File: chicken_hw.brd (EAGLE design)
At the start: 25.7 x 38.1 mm, 3 parts

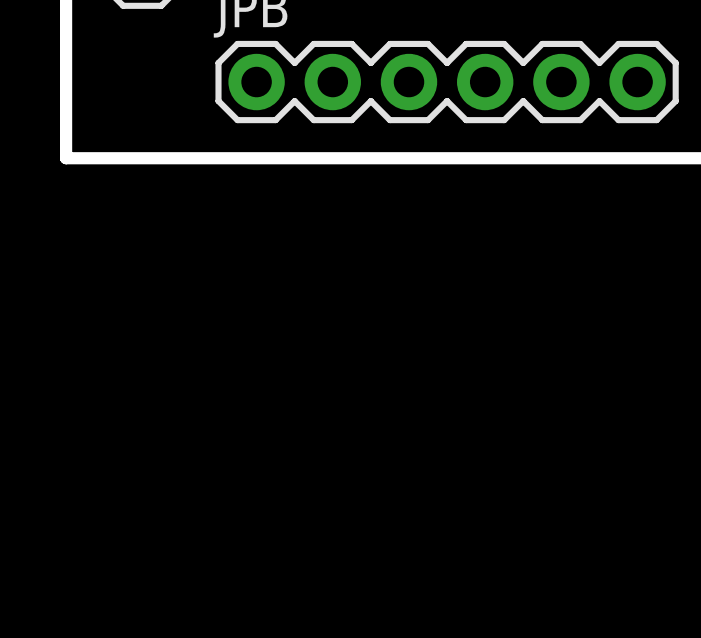
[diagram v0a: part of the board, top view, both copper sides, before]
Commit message: Start adding analog mux to design
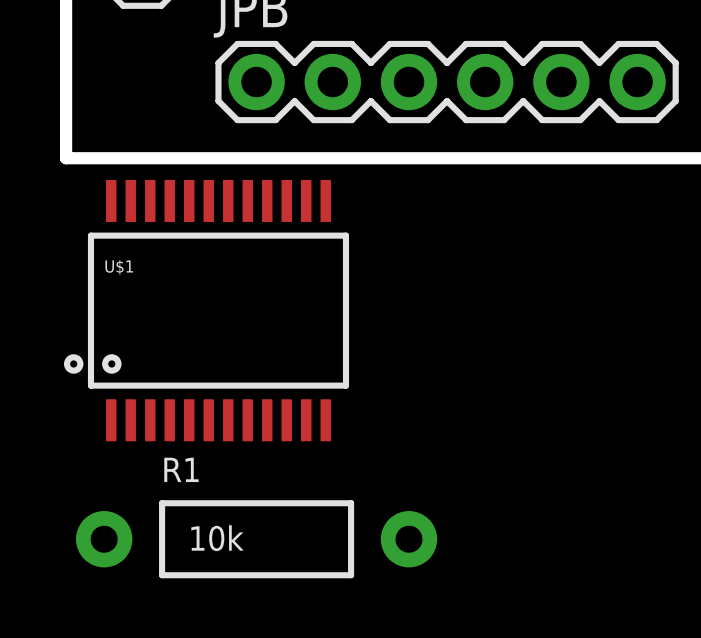
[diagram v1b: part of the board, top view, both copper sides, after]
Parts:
- added R1: 10k, SparkFun-Resistors:AXIAL-0.4
- added U$1: MUX-74HC4067SMD, SparkFun-AnalogIC:SSOP24
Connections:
- removed net GPIO2: JPR.6
- new net EN_MUX: JPR.6, R1.P$1, U$1.15
- net 3.3V: now also R1.P$2, U$1.24
- net GND: now also U$1.12
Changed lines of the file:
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@@
 <attribute name="PROD_ID" value="CONN-11563" x="22.86" y="30.48" size="1.778" layer="27" rot="R270" display="off"/>
 </element>
+<element name="U$1" library="SparkFun-AnalogIC" package="SSOP24" value="MUX-74HC4067SMD" x="5.08" y="-5.08">
+<attribute name="PROD_ID" value="IC-08252" x="5.08" y="-5.08" size="1.778" layer="27" display="off"/>
+</element>
+<element name="R1" library="SparkFun-Resistors" package="AXIAL-0.4" value="10k" x="6.35" y="-12.7"/>
 </elements>
 <signals>
@@
 <contactref element="JPR" pad="7"/>
 </signal>
-<signal name="GPIO2">
-<contactref element="JPR" pad="6"/>
-</signal>
 <signal name="GPIO0">
 <contactref element="JPR" pad="5"/>
@@
 <contactref element="JPB" pad="6"/>
 <contactref element="JPL" pad="10"/>
+<contactref element="U$1" pad="12"/>
 <wire x1="19.05" y1="2.54" x2="22.86" y2="7.62" width="0" layer="19" extent="1-1"/>
-<wire x1="2.54" y1="6.35" x2="19.05" y2="2.54" width="0" layer="19" extent="1-1"/>
+<wire x1="8.655" y1="-8.736" x2="19.05" y2="2.54" width="0" layer="19" extent="1-1"/>
+<wire x1="2.54" y1="6.35" x2="8.655" y2="-8.736" width="0" layer="19" extent="1-1"/>
 </signal>
 <signal name="N$11">
@@
 <signal name="3.3V">
 <contactref element="JPR" pad="8"/>
+<contactref element="U$1" pad="24"/>
+<contactref element="R1" pad="P$2"/>
+<wire x1="1.505" y1="-1.424" x2="22.86" y2="12.7" width="0" layer="19" extent="1-1"/>
+<wire x1="11.43" y1="-12.7" x2="1.505" y2="-1.424" width="0" layer="19" extent="1-1"/>
+</signal>
+<signal name="EN_MUX">
+<contactref element="U$1" pad="15"/>
+<contactref element="R1" pad="P$1"/>
+<contactref element="JPR" pad="6"/>
+<wire x1="7.355" y1="-1.424" x2="22.86" y2="17.78" width="0" layer="19" extent="1-1"/>
+<wire x1="1.27" y1="-12.7" x2="7.355" y2="-1.424" width="0" layer="19" extent="1-1"/>
 </signal>
 </signals>

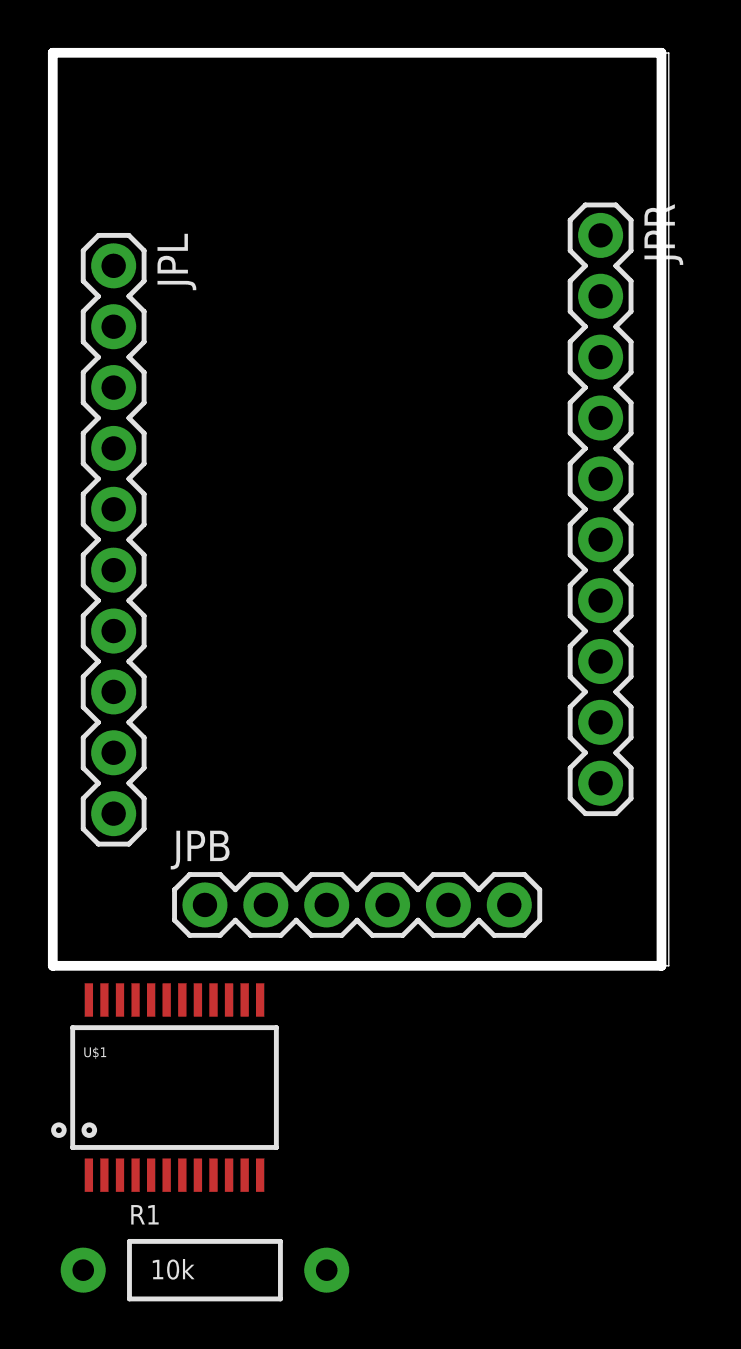
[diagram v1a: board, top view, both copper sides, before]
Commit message: Rough placement of components on board design
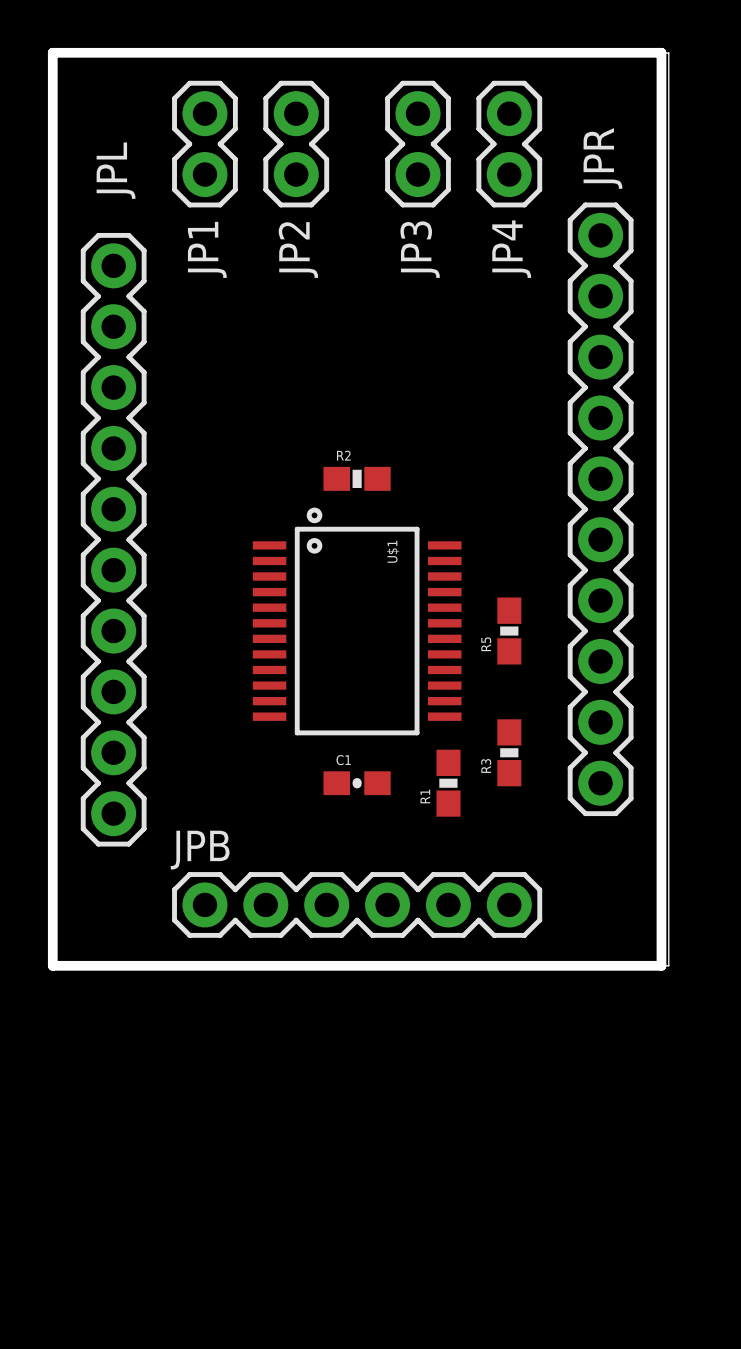
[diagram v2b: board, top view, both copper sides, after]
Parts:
- added C1: (no value), SparkFun-Capacitors:0603-CAP
- added JP1, JP2, JP3, JP4: (no value), SparkFun-Connectors:1X02
- added R2: 238k, SparkFun-Resistors:0603-RES
- added R3, R5: 10k, SparkFun-Resistors:0603-RES
- R1: device SparkFun-Resistors:AXIAL-0.4 -> SparkFun-Resistors:0603-RES
- moved R1 22.7 mm to (16.5, 7.62), turned to 90 degrees
- moved U$1 20.5 mm to (12.7, 14.0), turned to 270 degrees
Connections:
- new net N$1: R1.2, U$1.13
- new net N$2: JP1.2, U$1.9
- new net N$3: JP2.2, U$1.8
- new net N$4: JP3.2, U$1.7
- new net N$5: JP4.2, U$1.6
- new net N$6: R3.2, U$1.14
- net 3.3V: now also C1.1, R2.2, R5.2; no longer R1.P$2
- net A: now also R2.1, U$1.1
- net EN_MUX: now also R5.1; no longer R1.P$1
- net GND: now also C1.2, JP1.1, JP2.1, JP3.1, JP4.1, R1.1, R3.1
- net GPIO4: now also U$1.10
- net GPIO5: now also U$1.11
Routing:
- added copper zone on layer 1, net GND
- added copper zone on layer 16, net GND
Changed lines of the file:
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@@
 <layer number="112" name="tSilk" color="7" fill="1" visible="no" active="yes"/>
 <layer number="113" name="IDFDebug" color="4" fill="1" visible="no" active="yes"/>
+<layer number="114" name="Badge_Outline" color="7" fill="1" visible="yes" active="yes"/>
+<layer number="115" name="ReferenceISLANDS" color="7" fill="1" visible="yes" active="yes"/>
 <layer number="116" name="Patch_BOT" color="9" fill="4" visible="no" active="yes"/>
 <layer number="118" name="Rect_Pads" color="7" fill="1" visible="yes" active="yes"/>
@@
 <attribute name="PROD_ID" value="CONN-08437" x="34.29" y="0" size="1.778" layer="27" display="off"/>
 </element>
-<element name="JPL" library="SparkFun-Connectors" package="1X10" value="" x="2.54" y="29.21" rot="R270">
+<element name="JPL" library="SparkFun-Connectors" package="1X10" value="" x="2.54" y="29.21" smashed="yes" rot="R270">
 <attribute name="PROD_ID" value="CONN-11563" x="2.54" y="29.21" size="1.778" layer="27" rot="R270" display="off"/>
-</element>
-<element name="JPR" library="SparkFun-Connectors" package="1X10" value="" x="22.86" y="30.48" rot="R270">
+<attribute name="NAME" x="1.8288" y="34.3662" size="1.27" layer="25" ratio="10" rot="R270"/>
+<attribute name="VALUE" x="-0.635" y="30.48" size="1.27" layer="27" rot="R270"/>
+</element>
+<element name="JPR" library="SparkFun-Connectors" package="1X10" value="" x="22.86" y="30.48" smashed="yes" rot="R270">
 <attribute name="PROD_ID" value="CONN-11563" x="22.86" y="30.48" size="1.778" layer="27" rot="R270" display="off"/>
-</element>
-<element name="U$1" library="SparkFun-AnalogIC" package="SSOP24" value="MUX-74HC4067SMD" x="5.08" y="-5.08">
-<attribute name="PROD_ID" value="IC-08252" x="5.08" y="-5.08" size="1.778" layer="27" display="off"/>
-</element>
-<element name="R1" library="SparkFun-Resistors" package="AXIAL-0.4" value="10k" x="6.35" y="-12.7"/>
+<attribute name="NAME" x="22.1488" y="35.0012" size="1.27" layer="25" ratio="10" rot="R270"/>
+<attribute name="VALUE" x="19.685" y="31.75" size="1.27" layer="27" rot="R270"/>
+</element>
+<element name="U$1" library="SparkFun-AnalogIC" package="SSOP24" value="MUX-74HC4067SMD" x="12.7" y="13.97" rot="R270">
+<attribute name="PROD_ID" value="IC-08252" x="12.7" y="13.97" size="1.778" layer="27" rot="R270" display="off"/>
+</element>
+<element name="JP1" library="SparkFun-Connectors" package="1X02" value="" x="6.35" y="35.56" smashed="yes" rot="R270">
+<attribute name="NAME" x="5.6388" y="31.1912" size="1.27" layer="25" ratio="10" rot="R270"/>
+<attribute name="VALUE" x="3.175" y="36.83" size="1.27" layer="27" rot="R270"/>
+</element>
+<element name="JP2" library="SparkFun-Connectors" package="1X02" value="" x="10.16" y="35.56" smashed="yes" rot="R270">
+<attribute name="NAME" x="9.4488" y="31.1912" size="1.27" layer="25" ratio="10" rot="R270"/>
+<attribute name="VALUE" x="6.985" y="36.83" size="1.27" layer="27" rot="R270"/>
+</element>
+<element name="JP3" library="SparkFun-Connectors" package="1X02" value="" x="15.24" y="35.56" smashed="yes" rot="R270">
+<attribute name="NAME" x="14.5288" y="31.1912" size="1.27" layer="25" ratio="10" rot="R270"/>
+<attribute name="VALUE" x="12.065" y="36.83" size="1.27" layer="27" rot="R270"/>
+</element>
+<element name="JP4" library="SparkFun-Connectors" package="1X02" value="" x="19.05" y="35.56" smashed="yes" rot="R270">
+<attribute name="NAME" x="18.3388" y="31.1912" size="1.27" layer="25" ratio="10" rot="R270"/>
+<attribute name="VALUE" x="15.875" y="36.83" size="1.27" layer="27" rot="R270"/>
+</element>
+<element name="C1" library="SparkFun-Capacitors" package="0603-CAP" value="" x="12.7" y="7.62"/>
+<element name="R5" library="SparkFun-Resistors" package="0603-RES" value="10k" x="19.05" y="13.97" rot="R90"/>
+<element name="R1" library="SparkFun-Resistors" package="0603-RES" value="10k" x="16.51" y="7.62" rot="R90"/>
+<element name="R3" library="SparkFun-Resistors" package="0603-RES" value="10k" x="19.05" y="8.89" rot="R90"/>
+<element name="R2" library="SparkFun-Resistors" package="0603-RES" value="238k" x="12.7" y="20.32"/>
 </elements>
 <signals>
@@
 <signal name="A">
 <contactref element="JPL" pad="2"/>
+<contactref element="U$1" pad="1"/>
+<contactref element="R2" pad="1"/>
+<wire x1="9.044" y1="17.545" x2="11.85" y2="20.32" width="0" layer="19" extent="1-1"/>
+<wire x1="2.54" y1="26.67" x2="9.044" y2="17.545" width="0" layer="19" extent="1-1"/>
 </signal>
 <signal name="EN">
@@
 <signal name="GPIO4">
 <contactref element="JPR" pad="4"/>
+<contactref element="U$1" pad="10"/>
+<wire x1="9.044" y1="11.695" x2="22.86" y2="22.86" width="0" layer="19" extent="1-1"/>
 </signal>
 <signal name="GPIO5">
 <contactref element="JPR" pad="3"/>
+<contactref element="U$1" pad="11"/>
+<wire x1="9.044" y1="11.045" x2="22.86" y2="25.4" width="0" layer="19" extent="1-1"/>
 </signal>
 <signal name="RX_R">
@@
 <contactref element="JPL" pad="10"/>
 <contactref element="U$1" pad="12"/>
-<wire x1="19.05" y1="2.54" x2="22.86" y2="7.62" width="0" layer="19" extent="1-1"/>
-<wire x1="8.655" y1="-8.736" x2="19.05" y2="2.54" width="0" layer="19" extent="1-1"/>
-<wire x1="2.54" y1="6.35" x2="8.655" y2="-8.736" width="0" layer="19" extent="1-1"/>
+<contactref element="JP1" pad="1"/>
+<contactref element="JP2" pad="1"/>
+<contactref element="JP3" pad="1"/>
+<contactref element="JP4" pad="1"/>
+<contactref element="C1" pad="2"/>
+<polygon width="0.4064" layer="1">
+<vertex x="0" y="38.1"/>
+<vertex x="0" y="0"/>
+<vertex x="25.4" y="0"/>
+<vertex x="25.4" y="38.1"/>
+</polygon>
+<polygon width="0.4064" layer="16">
+<vertex x="0" y="38.1"/>
+<vertex x="0" y="0"/>
+<vertex x="25.4" y="0"/>
+<vertex x="25.4" y="38.1"/>
+</polygon>
+<contactref element="R1" pad="1"/>
+<contactref element="R3" pad="1"/>
 </signal>
 <signal name="N$11">
@@
 <contactref element="JPR" pad="8"/>
 <contactref element="U$1" pad="24"/>
-<contactref element="R1" pad="P$2"/>
-<wire x1="1.505" y1="-1.424" x2="22.86" y2="12.7" width="0" layer="19" extent="1-1"/>
-<wire x1="11.43" y1="-12.7" x2="1.505" y2="-1.424" width="0" layer="19" extent="1-1"/>
+<contactref element="C1" pad="1"/>
+<contactref element="R5" pad="2"/>
+<contactref element="R2" pad="2"/>
+<wire x1="19.05" y1="14.82" x2="22.86" y2="12.7" width="0" layer="19" extent="1-1"/>
+<wire x1="16.356" y1="17.545" x2="19.05" y2="14.82" width="0" layer="19" extent="1-1"/>
+<wire x1="13.55" y1="20.32" x2="16.356" y2="17.545" width="0" layer="19" extent="1-1"/>
+<wire x1="11.85" y1="7.62" x2="19.05" y2="14.82" width="0" layer="19" extent="1-1"/>
 </signal>
 <signal name="EN_MUX">
 <contactref element="U$1" pad="15"/>
-<contactref element="R1" pad="P$1"/>
 <contactref element="JPR" pad="6"/>
-<wire x1="7.355" y1="-1.424" x2="22.86" y2="17.78" width="0" layer="19" extent="1-1"/>
-<wire x1="1.27" y1="-12.7" x2="7.355" y2="-1.424" width="0" layer="19" extent="1-1"/>
+<contactref element="R5" pad="1"/>
+<wire x1="19.05" y1="13.12" x2="22.86" y2="17.78" width="0" layer="19" extent="1-1"/>
+<wire x1="16.356" y1="11.695" x2="19.05" y2="13.12" width="0" layer="19" extent="1-1"/>
+</signal>
+<signal name="N$2">
+<contactref element="JP1" pad="2"/>
+<contactref element="U$1" pad="9"/>
+<wire x1="9.044" y1="12.345" x2="6.35" y2="33.02" width="0" layer="19" extent="1-1"/>
+</signal>
+<signal name="N$3">
+<contactref element="JP2" pad="2"/>
+<contactref element="U$1" pad="8"/>
+<wire x1="9.044" y1="12.995" x2="10.16" y2="33.02" width="0" layer="19" extent="1-1"/>
+</signal>
+<signal name="N$4">
+<contactref element="JP3" pad="2"/>
+<contactref element="U$1" pad="7"/>
+<wire x1="9.044" y1="13.645" x2="15.24" y2="33.02" width="0" layer="19" extent="1-1"/>
+</signal>
+<signal name="N$5">
+<contactref element="JP4" pad="2"/>
+<contactref element="U$1" pad="6"/>
+<wire x1="9.044" y1="14.295" x2="19.05" y2="33.02" width="0" layer="19" extent="1-1"/>
+</signal>
+<signal name="N$1">
+<contactref element="U$1" pad="13"/>
+<contactref element="R1" pad="2"/>
+<wire x1="16.51" y1="8.47" x2="16.356" y2="10.395" width="0" layer="19" extent="1-1"/>
+</signal>
+<signal name="N$6">
+<contactref element="U$1" pad="14"/>
+<contactref element="R3" pad="2"/>
+<wire x1="19.05" y1="9.74" x2="16.356" y2="11.045" width="0" layer="19" extent="1-1"/>
 </signal>
 </signals>

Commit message: Add connector text to board design
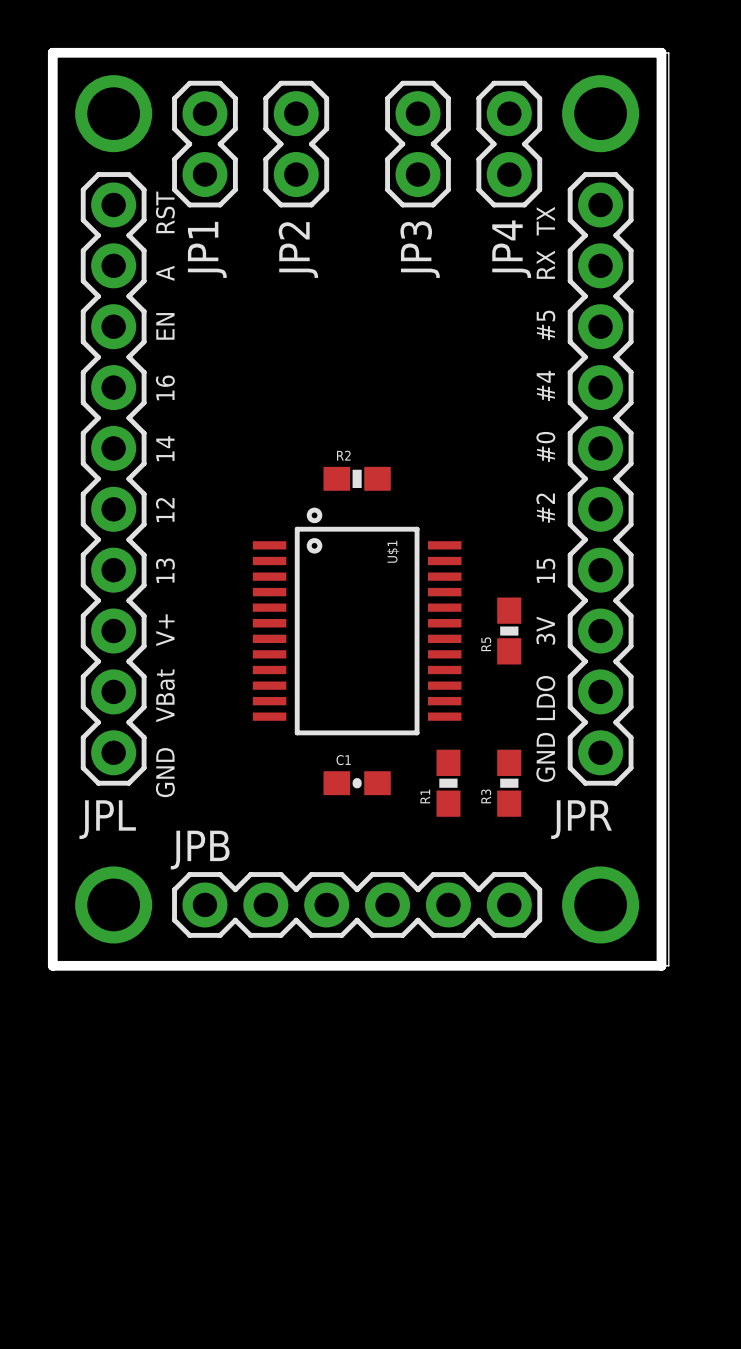
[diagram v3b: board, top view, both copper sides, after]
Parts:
- moved JPL 2.54 mm to (2.54, 31.8)
- moved R3 1.27 mm to (19.1, 7.62)
- moved JPR 1.27 mm to (22.9, 31.8)
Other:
- board text added: "#0"
- board text added: "#2"
- board text added: "#4"
- board text added: "#5"
- board text added: "12"
- board text added: "13"
- board text added: "14"
- board text added: "15"
- board text added: "16"
- board text added: "3V"
- board text added: "A"
- board text added: "EN"
- board text added: "GND"
- board text added: "LDO"
- board text added: "RST"
- board text added: "RX"
- board text added: "TX"
- board text added: "V+"
- board text added: "VBat"
